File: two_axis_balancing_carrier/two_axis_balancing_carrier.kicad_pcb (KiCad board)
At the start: 0 parts

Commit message: Power actually finished; carrier pcb started
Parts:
- added C1: 470pF, Capacitor_SMD:C_0603_1608Metric, F.Cu at (54.3, 43.5)
- added C2: 2.2uF, Capacitor_SMD:C_0805_2012Metric, F.Cu at (54.6, 75.1)
- added C3: 100nF, Capacitor_SMD:C_0603_1608Metric, F.Cu at (54.3, 46.0)
- added C4: 10nF, Capacitor_SMD:C_0603_1608Metric, F.Cu at (54.3, 48.5)
- added C5: 100nF, Capacitor_SMD:C_0603_1608Metric, F.Cu at (54.3, 51.0)
- added C6: 2.2uF, Capacitor_SMD:C_0805_2012Metric, F.Cu at (54.6, 78.1)
- added J1: Conn_01x03, Connector_PinSocket_2.54mm:PinSocket_1x03_P2.54mm_Vertical, F.Cu at (54.6, 59.6)
- added J2: Conn_01x04, Connector_PinSocket_2.54mm:PinSocket_1x04_P2.54mm_Vertical, F.Cu at (71.5, 140.8)
- added J5: Conn_02x05, Connector_IDC:IDC-Header_2x05_P2.54mm_Vertical, F.Cu at (75.9, 102.3)
- added R1: 120R, Resistor_SMD:R_0603_1608Metric, F.Cu at (54.3, 53.5)
- added R2: 120R, Resistor_SMD:R_0603_1608Metric, F.Cu at (54.3, 56.0)
- added U1: NUCLEO-G474RE, NUCLEO-G474:MODULE_NUCLEO-G474RE, F.Cu at (133.8, 97.4)
- added U2: MIC5219-3.3YM5, Package_TO_SOT_SMD:SOT-23-5, F.Cu at (59.4, 76.0)
- added U3: ICM-42688-P, ICM:LGA14_2P5X3X0P91_TDK, F.Cu at (54.7, 81.6)
- added U4: SN65HVD230, Package_SO:SOIC-8_3.9x4.9mm_P1.27mm, F.Cu at (56.6, 70.3)
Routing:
- net /AIN1: track 0.00 -> 133.0 mm
- net /ENC_A: track 0.00 -> 113.8 mm
- net /BAT_LOW: track 0.00 -> 106.1 mm
- net /AIN2: track 0.00 -> 90.3 mm
- net /PWMA: track 0.00 -> 67.4 mm
- net /STBY: track 0.00 -> 47.1 mm
- net /BAT_LEV: track 0.00 -> 37.4 mm
- net +5V: track 0.00 -> 32.5 mm
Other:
- board outline added: 106.6 x 94.9 mm
- copper layers 0 -> 4

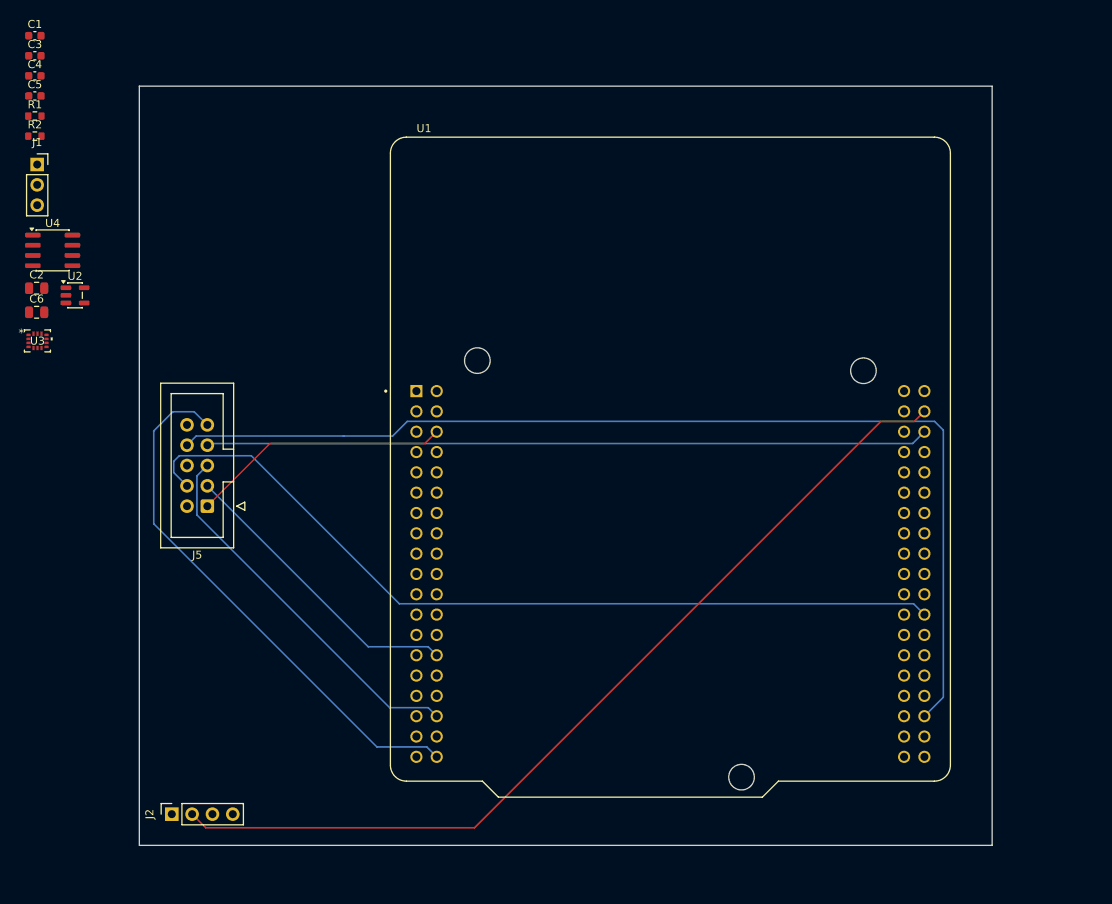
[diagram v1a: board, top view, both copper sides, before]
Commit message: Carrier layout finished
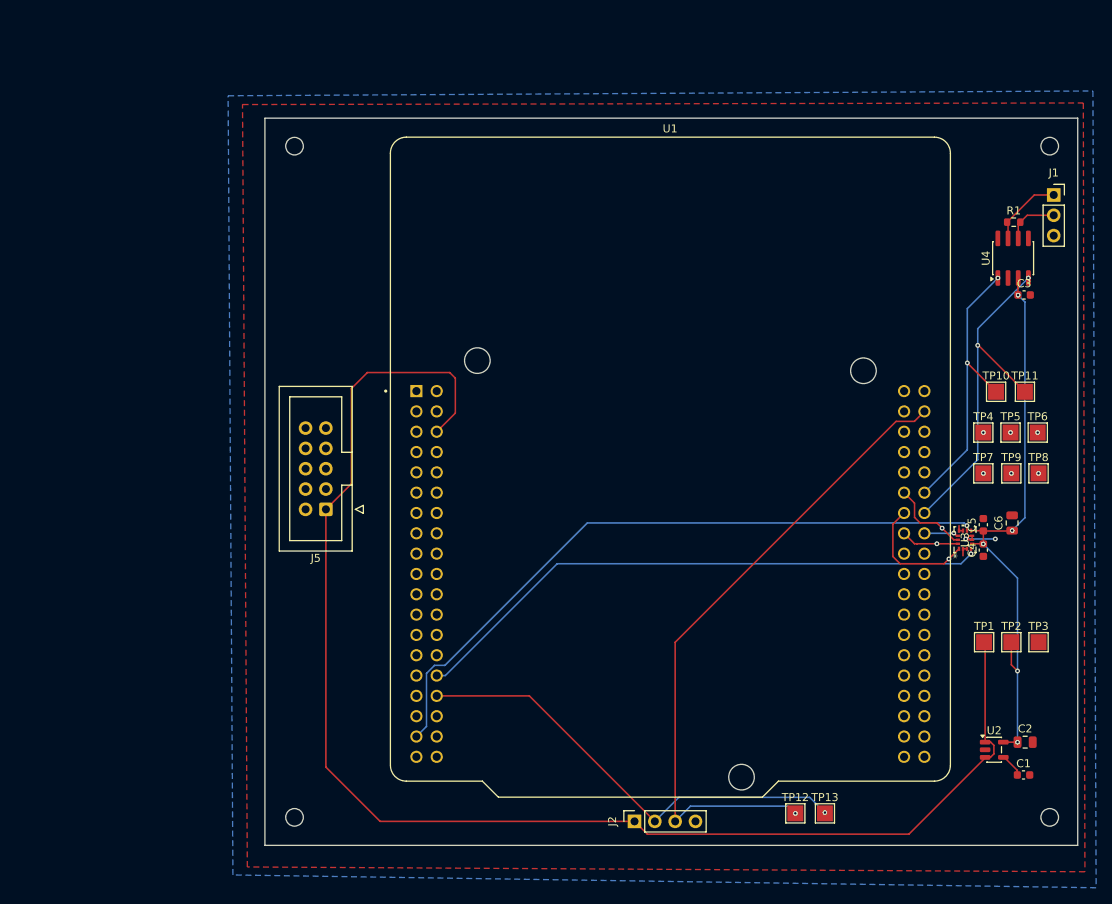
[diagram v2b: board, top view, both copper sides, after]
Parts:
- removed R2: 120R, Resistor_SMD:R_0603_1608Metric
- added REF**: MountingHole_2.2mm_M2, MountingHole:MountingHole_2.2mm_M2, F.Cu at (86.8, 141.2)
- added REF**: MountingHole_2.2mm_M2, MountingHole:MountingHole_2.2mm_M2, F.Cu at (181.2, 57.3)
- added REF**: MountingHole_2.2mm_M2, MountingHole:MountingHole_2.2mm_M2, F.Cu at (86.8, 57.3)
- added REF**: MountingHole_2.2mm_M2, MountingHole:MountingHole_2.2mm_M2, F.Cu at (181.2, 141.2)
- added TP1: TestPoint, TestPoint:TestPoint_Pad_2.0x2.0mm, F.Cu at (173.0, 119.3)
- added TP10: TestPoint, TestPoint:TestPoint_Pad_2.0x2.0mm, F.Cu at (174.5, 88.0)
- added TP11: TestPoint, TestPoint:TestPoint_Pad_2.0x2.0mm, F.Cu at (178.1, 88.0)
- added TP12: TestPoint, TestPoint:TestPoint_Pad_2.0x2.0mm, F.Cu at (149.4, 140.7)
- added TP13: TestPoint, TestPoint:TestPoint_Pad_2.0x2.0mm, F.Cu at (153.1, 140.7)
- added TP2: TestPoint, TestPoint:TestPoint_Pad_2.0x2.0mm, F.Cu at (176.4, 119.3)
- added TP3: TestPoint, TestPoint:TestPoint_Pad_2.0x2.0mm, F.Cu at (179.8, 119.3)
- added TP4: TestPoint, TestPoint:TestPoint_Pad_2.0x2.0mm, F.Cu at (172.9, 93.1)
- added TP5: TestPoint, TestPoint:TestPoint_Pad_2.0x2.0mm, F.Cu at (176.3, 93.1)
- added TP6: TestPoint, TestPoint:TestPoint_Pad_2.0x2.0mm, F.Cu at (179.7, 93.1)
- added TP7: TestPoint, TestPoint:TestPoint_Pad_2.0x2.0mm, F.Cu at (172.9, 98.2)
- added TP8: TestPoint, TestPoint:TestPoint_Pad_2.0x2.0mm, F.Cu at (179.8, 98.2)
- added TP9: TestPoint, TestPoint:TestPoint_Pad_2.0x2.0mm, F.Cu at (176.4, 98.2)
- moved C1 154.3 mm to (177.9, 135.9)
- moved C2 136.0 mm to (178.1, 131.8)
- moved C4 132.6 mm to (172.9, 107.8), turned to 90 degrees
- moved C5 130.1 mm to (172.9, 104.6), turned to 90 degrees
- moved U2 128.2 mm to (174.3, 132.8)
- moved C3 127.2 mm to (178.0, 75.9)
- moved J1 127.1 mm to (181.7, 63.4)
- moved C6 124.7 mm to (176.5, 104.4), turned to 90 degrees
- moved R1 123.1 mm to (176.7, 66.8)
- moved U4 120.1 mm to (176.6, 71.3), turned to 90 degrees
- moved U3 118.6 mm to (170.6, 106.5), turned to 90 degrees
- moved J2 57.8 mm to (129.3, 141.7)
- moved J5 14.8 mm to (90.7, 102.7)
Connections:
- J2 pad 2: /ENC_A -> /ENC_B
- J2 pad 3: /ENC_B -> /ENC_A
- U1 pad CN10_12: unconnected-(U1B-PA12-PadCN10_12) -> /TX
- U1 pad CN10_14: unconnected-(U1B-PA11-PadCN10_14) -> /RX
- U1 pad CN10_16: unconnected-(U1B-PB12-PadCN10_16) -> /CS
- U1 pad CN10_24: /BAT_LOW -> unconnected-(U1B-PB1-PadCN10_24)
- U1 pad CN10_32: unconnected-(U1B-AGND-PadCN10_32) -> GND
- U1 pad CN10_34: /AIN1 -> unconnected-(U1B-PC4-PadCN10_34)
- U1 pad CN10_6: /AIN2 -> unconnected-(U1B-PC5-PadCN10_6)
- U1 pad CN7_23: unconnected-(U1A-PC13-PadCN7_23) -> /AIN1
- U1 pad CN7_25: unconnected-(U1A-PC14-PadCN7_25) -> /AIN2
- U1 pad CN7_27: unconnected-(U1A-PC15-PadCN7_27) -> /STBY
- U1 pad CN7_34: /STBY -> unconnected-(U1A-PB0-PadCN7_34)
- U1 pad CN7_37: unconnected-(U1A-PC3-PadCN7_37) -> /BAT_LOW
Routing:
- net +5V: track 32.5 -> 176.5 mm
- net /AIN1: track 133.0 -> 32.8 mm
- net /INT2: track 0.00 -> 93.4 mm, vias 0 -> 2
- net /INT1: track 0.00 -> 87.6 mm, vias 0 -> 2
- net +3.3V: track 0.00 -> 73.1 mm, vias 0 -> 5
- net /BAT_LOW: track 106.1 -> 40.4 mm
- net /AIN2: track 90.3 -> 30.1 mm
- net /ENC_B: track 0.00 -> 57.1 mm, vias 0 -> 1
- net /RX: track 0.00 -> 43.1 mm, vias 0 -> 2
- net /SDO: track 0.00 -> 38.3 mm, vias 0 -> 2
- net /TX: track 0.00 -> 35.7 mm, vias 0 -> 2
- net /ENC_A: track 113.8 -> 81.7 mm, vias 0 -> 1
- net /SCLK: track 0.00 -> 27.0 mm, vias 0 -> 2
- net /SDI: track 0.00 -> 23.6 mm, vias 0 -> 2
- net /STBY: track 47.1 -> 29.5 mm
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- added copper zone on B.Cu, net GND
- added copper zone on F.Cu, net GND
- added copper zone on In1.Cu, net GND
- added copper zone on In2.Cu, net GND
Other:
- board size 106.6 x 94.9 mm -> 101.6 x 90.9 mm
